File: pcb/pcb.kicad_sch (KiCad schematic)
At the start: 49 parts, among them SW1 MX_SWITCH, SW10 MX_SWITCH, SW11 MX_SWITCH, SW12 MX_SWITCH, SW13 MX_SWITCH, SW14 MX_SWITCH, SW15 MX_SWITCH, SW16 MX_SWITCH, SW2 MX_SWITCH, SW3 MX_SWITCH, SW4 RotaryEncoder_Switch, SW5 MX_SWITCH, SW6 MX_SWITCH, SW7 MX_SWITCH, SW8 MX_SWITCH, SW9 MX_SWITCH, U1 XIAO-RP2040-DIP

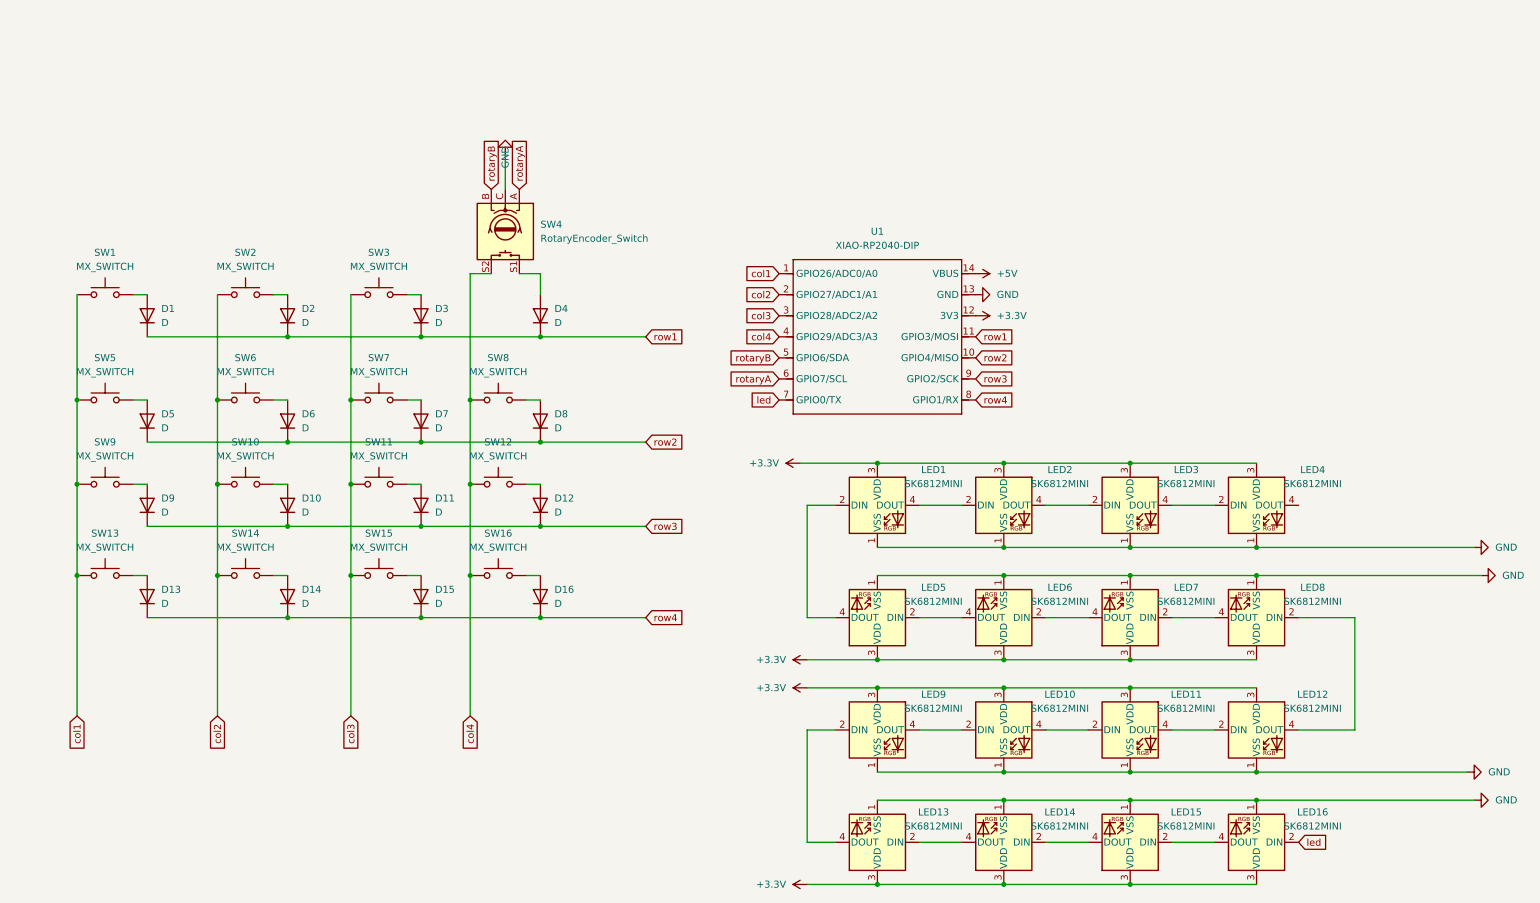
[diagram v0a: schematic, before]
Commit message: update schematics and footprints to match sk6812mini-e
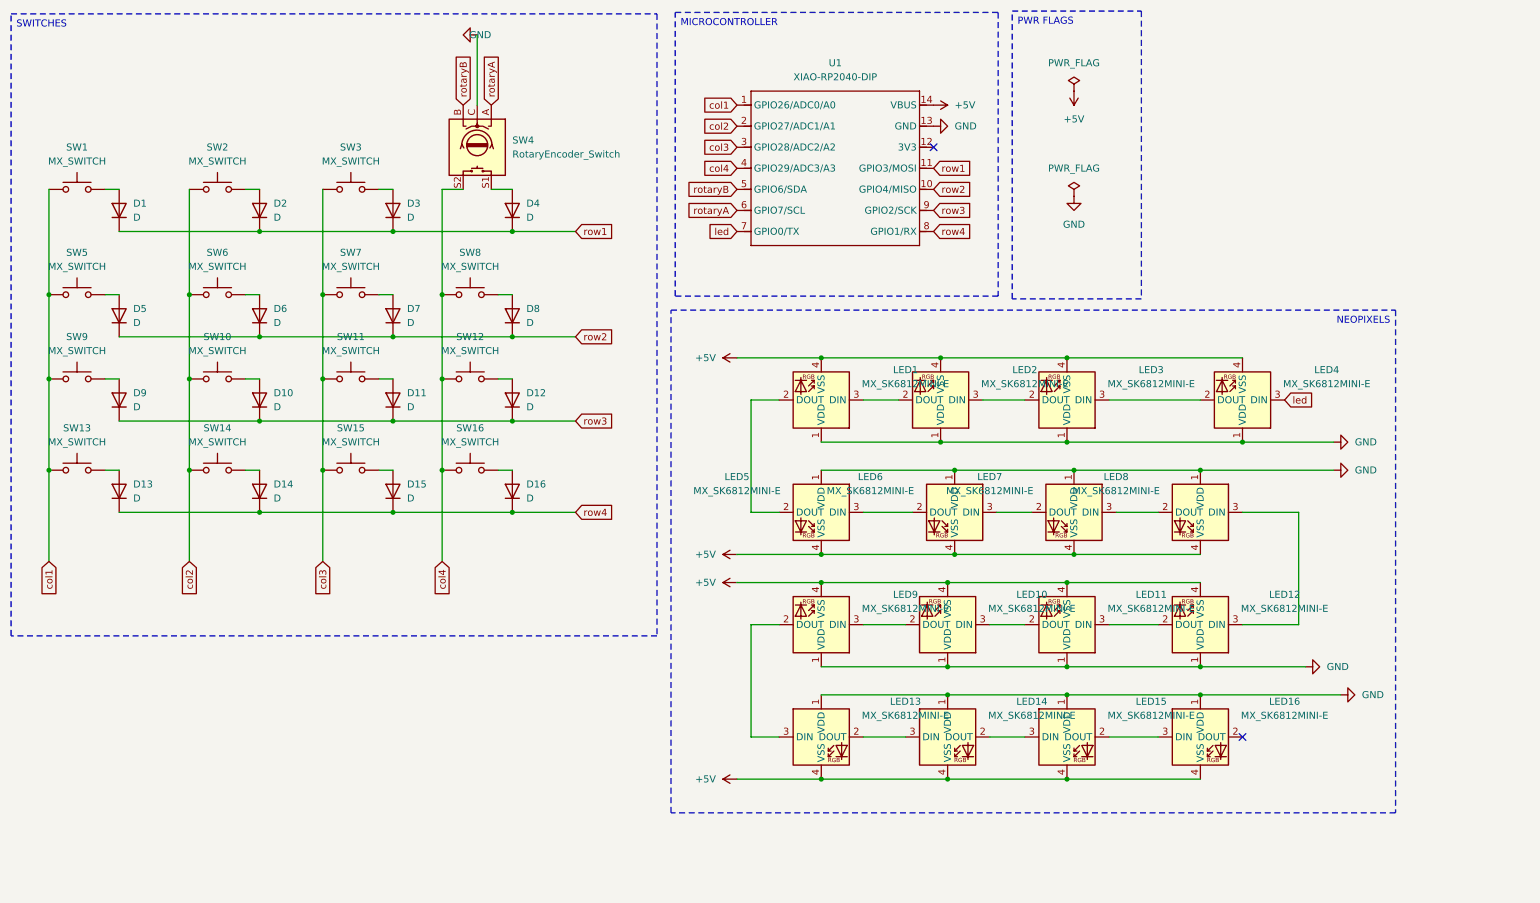
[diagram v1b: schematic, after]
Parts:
- removed LED1, LED10, LED11, LED12, LED13, LED14, LED15, LED16, LED2, LED3, LED4, LED5, LED6, LED7, LED8, LED9: SK6812MINI, LED_SMD:LED_SK6812MINI_PLCC4_3.5x3.5mm_P1.75mm, symbol LED:SK6812
- added LED1, LED10, LED11, LED12, LED13, LED14, LED15, LED16, LED2, LED3, LED4, LED5, LED6, LED7, LED8, LED9: MX_SK6812MINI-E, PCM_marbastlib-mx:LED_MX_6028R, symbol PCM_marbastlib-mx:MX_SK6812MINI-E
- SW1, SW10, SW11, SW12, SW13, SW14, SW15, SW16, SW2, SW3, SW5, SW6, SW7, SW8, SW9: footprint MX_Hotswap:MX-Hotswap-1U -> PCM_marbastlib-mx:SW_MX_HS_CPG151101S11_1u
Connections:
- net +5V: now also LED1.4 (VSS), LED10.4 (VSS), LED11.4 (VSS), LED12.4 (VSS), LED13.4 (VSS), LED14.4 (VSS), LED15.4 (VSS), LED16.4 (VSS), LED2.4 (VSS), LED3.4 (VSS), LED4.4 (VSS), LED5.4 (VSS), LED6.4 (VSS), LED7.4 (VSS), LED8.4 (VSS), LED9.4 (VSS)
- net GND: now also LED1.1 (VDD), LED10.1 (VDD), LED11.1 (VDD), LED12.1 (VDD), LED13.1 (VDD), LED14.1 (VDD), LED15.1 (VDD), LED16.1 (VDD), LED2.1 (VDD), LED3.1 (VDD), LED4.1 (VDD), LED5.1 (VDD), LED6.1 (VDD), LED7.1 (VDD), LED8.1 (VDD), LED9.1 (VDD)
- net led: now also LED4.3 (DIN)
- net +3.3V: no longer names the net of U1.12 (3V3)
- new net: LED10.2 (DOUT), LED9.3 (DIN)
- new net: LED10.3 (DIN), LED11.2 (DOUT)
- new net: LED15.2 (DOUT), LED16.3 (DIN)
- new net: LED11.3 (DIN), LED12.2 (DOUT)
- new net: LED12.3 (DIN), LED8.3 (DIN)
- new net: LED14.2 (DOUT), LED15.3 (DIN)
- new net: LED13.2 (DOUT), LED14.3 (DIN)
- new net: LED3.3 (DIN), LED4.2 (DOUT)
- new net: LED6.3 (DIN), LED7.2 (DOUT)
- new net: LED7.3 (DIN), LED8.2 (DOUT)
- new net: LED5.3 (DIN), LED6.2 (DOUT)
- new net: LED1.2 (DOUT), LED5.2 (DOUT)
- new net: LED13.3 (DIN), LED9.2 (DOUT)
- new net: LED1.3 (DIN), LED2.2 (DOUT)
- new net: LED2.3 (DIN), LED3.2 (DOUT)
- no-connect marks 0 -> 2
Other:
- moved on the sheet: D1, D10, D11, D12, D13, D14, D15, D16, D2, D3, D4, D5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
